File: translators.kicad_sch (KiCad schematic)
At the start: 53 parts, among them U10 SN74AXC8T245_UQFN, U2 SN74AXC8T245_UQFN, U3 SN74AXC8T245_UQFN, U4 SN74AXC8T245_UQFN, U5 SN74AXC8T245_UQFN, U6 SN74AXC8T245_UQFN

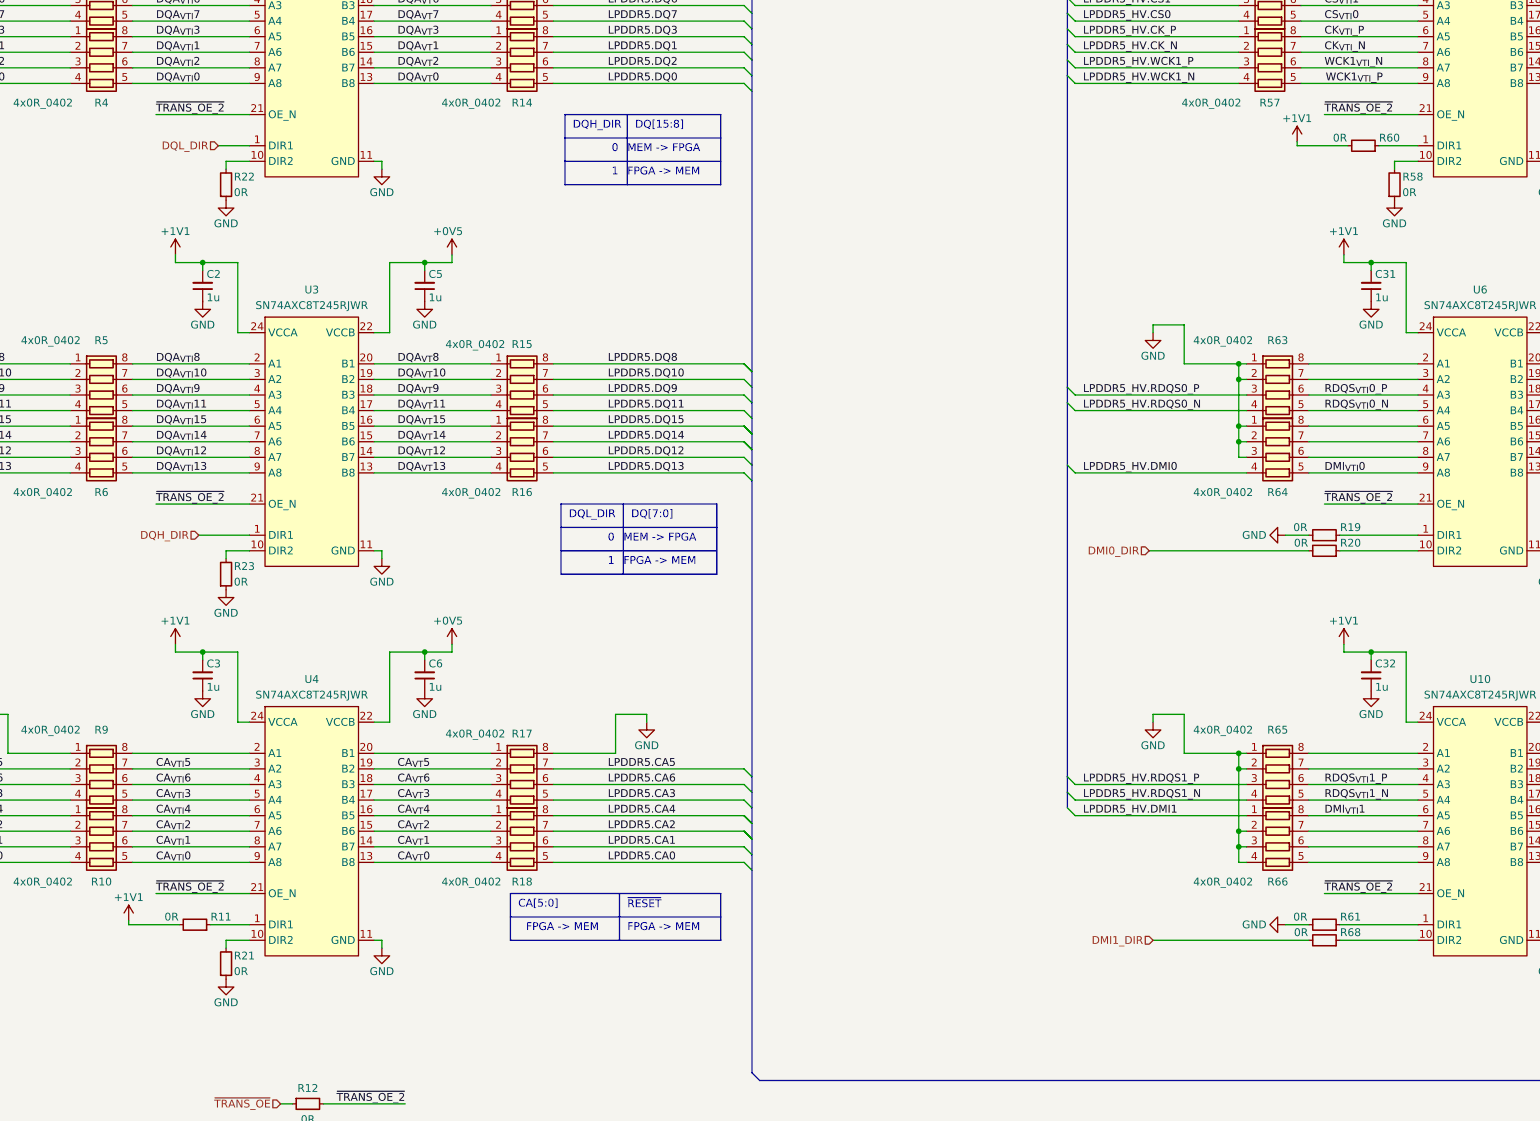
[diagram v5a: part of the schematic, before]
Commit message: [#52835] schematics: remove some 0R to simplify translator layout
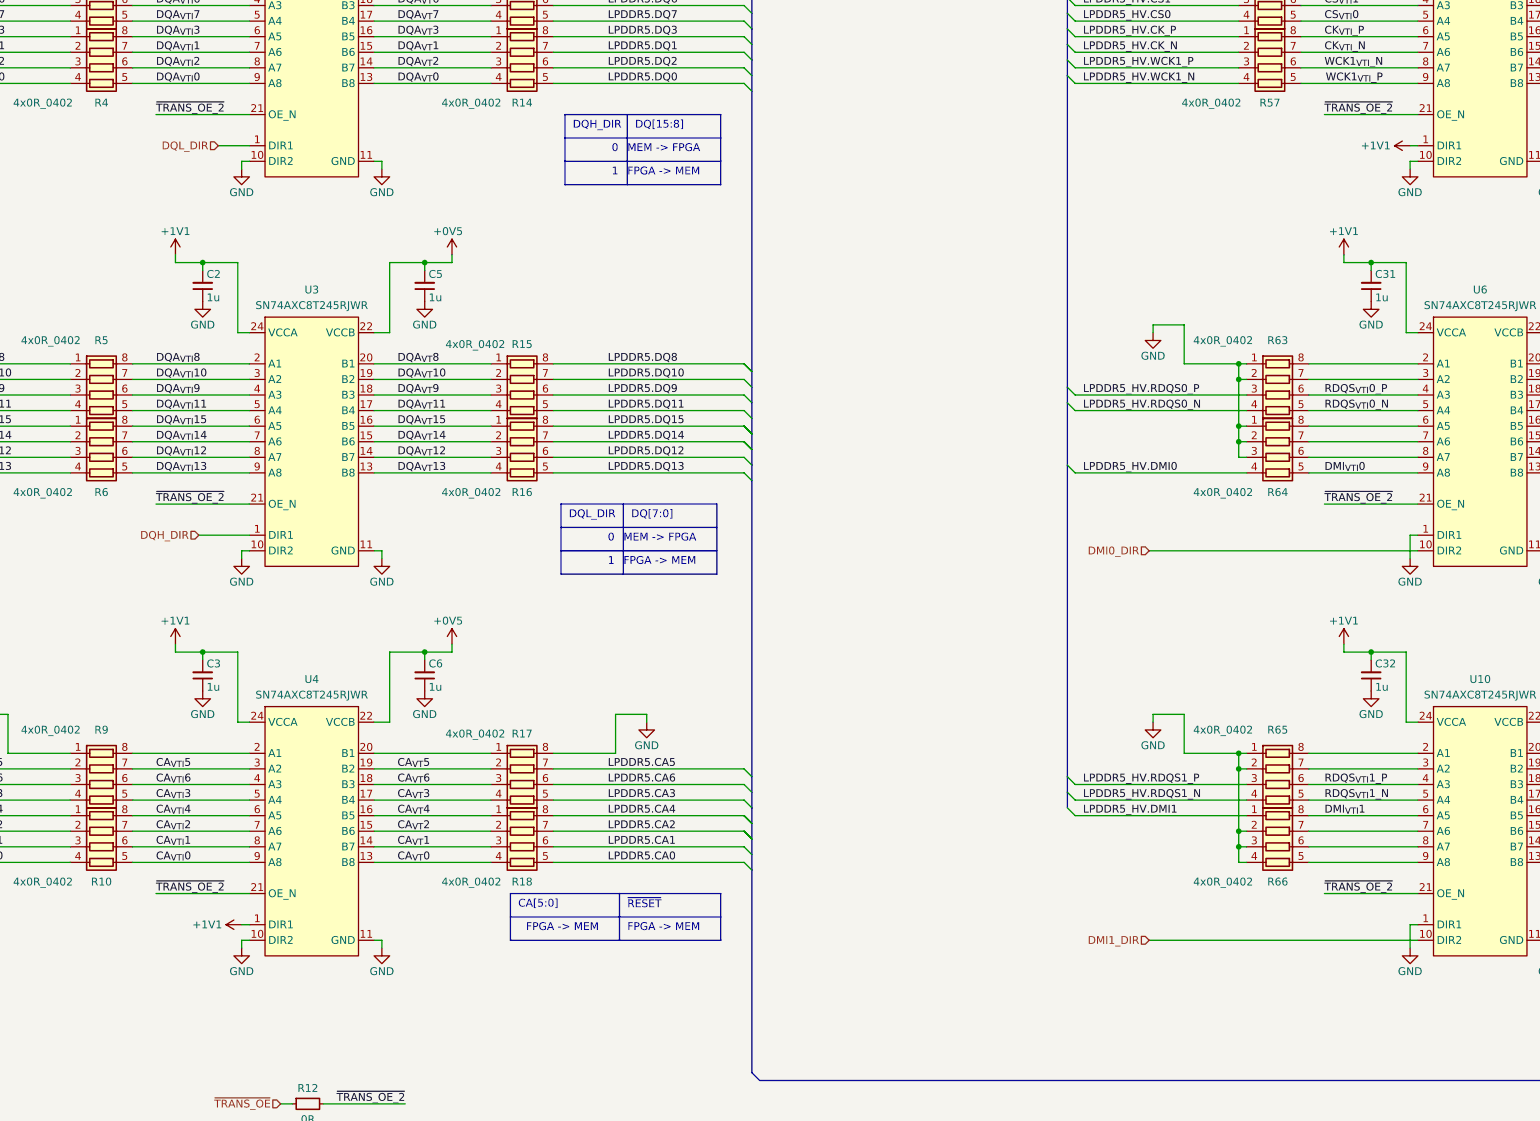
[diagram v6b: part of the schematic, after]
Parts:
- removed R11, R19, R20, R21, R22, R23, R58, R60, R61, R68: R_0R_0402, antmicro-footprints:R_0402_1005Metric, symbol antmicroResistors0402:R_0R_0402
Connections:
- net +1V1: now also U4.1 (DIR1), U5.1 (DIR1)
- net DMI0_DIR: now also U6.10 (DIR2)
- net DMI1_DIR: now also U10.10 (DIR2)
- net GND: now also U10.1 (DIR1), U2.10 (DIR2), U3.10 (DIR2), U4.10 (DIR2), U5.10 (DIR2), U6.1 (DIR1)

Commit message: [#52536] 52835: use resistors dividers instead of translators
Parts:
- removed C1, C2, C26, C3, C30, C31, C32, C33, C34, C4, C5, C6: C_1u_0402, antmicro-footprints:C_0402_1005Metric, symbol antmicroCapacitors0402:C_1u_0402
- removed R10, R13, R14, R15, R16, R17, R18, R24, R25, R3, R4, R48, R49, R5, R56, R57, R6, R63, R64, R65, R66, R7, R8, R9: 4x0R_0402_array, antmicro-footprints:4x0R_0402_array_EXB28V, symbol antmicroResistorNetworksArrays:4x0R_0402_array
- removed R12: R_0R_0402, antmicro-footprints:R_0402_1005Metric, symbol antmicroResistors0402:R_0R_0402
- removed U10, U2, U3, U4, U5, U6: SN74AXC8T245_UQFN, antmicro-footprints:UQFN-24_2x4mm_P0.4mm_Texas_RJW0024A, symbol antmicroLogicTranslatorsLevelShifters:SN74AXC8T245_UQFN
- added R15, R16, R17, R18, R19, R20, R21, R22, R23, R25, R3, R4, R49, R5, R54, R6, R64, R65, R66, R67, R7, R8: 4x100R_0201_array, antmicro-footprints:R_Array_4x0201_Panasonic_EXB18V, symbol antmicroResistorNetworksArrays:4x100R_0201_array
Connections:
- net GND: now also R18.5 (R4.2), R18.6 (R3.2), R18.7 (R2.2), R18.8 (R1.2), R25.1 (R1.1), R25.2 (R2.1), R25.3 (R3.1), R25.4 (R4.1), R3.5 (R4.2), R3.6 (R3.2), R3.7 (R2.2), R3.8 (R1.2), R4.1 (R1.1), R4.2 (R2.1), R4.3 (R3.1), R4.4 (R4.1), R49.1 (R1.1), R49.2 (R2.1), R49.3 (R3.1), R49.4 (R4.1), R5.1 (R1.1), R5.2 (R2.1), R5.3 (R3.1), R5.4 (R4.1), R6.1 (R1.1), R6.2 (R2.1), R6.3 (R3.1), R6.4 (R4.1), R66.1 (R1.1), R66.2 (R2.1), R66.3 (R3.1), R66.4 (R4.1), R67.1 (R1.1), R67.2 (R2.1), R67.3 (R3.1), R67.4 (R4.1), R7.1 (R1.1), R7.2 (R2.1), R7.3 (R3.1), R7.4 (R4.1), R8.1 (R1.1), R8.2 (R2.1), R8.3 (R3.1), R8.4 (R4.1)
- new net LPDDR5_DIE.CA0: R21.3 (R3.1), R5.6 (R3.2)
- new net LPDDR5_DIE.CA1: R21.4 (R4.1), R5.5 (R4.2)
- new net LPDDR5_DIE.CA2: R22.1 (R1.1), R6.8 (R1.2)
- new net LPDDR5_DIE.CA3: R22.2 (R2.1), R6.7 (R2.2)
- new net LPDDR5_DIE.CA4: R22.3 (R3.1), R6.6 (R3.2)
- new net LPDDR5_DIE.CA5: R22.4 (R4.1), R6.5 (R4.2)
- new net LPDDR5_DIE.CA6: R16.6 (R3.2), R3.3 (R3.1)
- new net LPDDR5_DIE.CK_N: R65.2 (R2.1), R67.7 (R2.2)
- new net LPDDR5_DIE.CK_P: R65.3 (R3.1), R67.6 (R3.2)
- new net LPDDR5_DIE.CS0: R20.4 (R4.1), R49.5 (R4.2)
- new net LPDDR5_DIE.CS1: R16.8 (R1.2), R3.1 (R1.1)
- new net LPDDR5_DIE.DMI0: R15.6 (R3.2), R18.3 (R3.1)
- new net LPDDR5_DIE.DMI1: R16.7 (R2.2), R3.2 (R2.1)
- new net LPDDR5_DIE.DQ0: R15.8 (R1.2), R18.1 (R1.1)
- new net LPDDR5_DIE.DQ1: R19.1 (R1.1), R25.8 (R1.2)
- new net LPDDR5_DIE.DQ10: R17.7 (R2.2), R4.7 (R2.2)
- new net LPDDR5_DIE.DQ11: R17.5 (R4.2), R4.5 (R4.2)
- new net LPDDR5_DIE.DQ12: R23.6 (R3.2), R7.6 (R3.2)
- new net LPDDR5_DIE.DQ13: R23.5 (R4.2), R7.5 (R4.2)
- new net LPDDR5_DIE.DQ14: R23.7 (R2.2), R7.7 (R2.2)
- new net LPDDR5_DIE.DQ15: R23.8 (R1.2), R7.8 (R1.2)
- new net LPDDR5_DIE.DQ2: R15.7 (R2.2), R18.2 (R2.1)
- new net LPDDR5_DIE.DQ3: R19.2 (R2.1), R25.7 (R2.2)
- new net LPDDR5_DIE.DQ4: R15.5 (R4.2), R18.4 (R4.1)
- new net LPDDR5_DIE.DQ5: R20.1 (R1.1), R49.8 (R1.2)
- new net LPDDR5_DIE.DQ6: R20.2 (R2.1), R49.7 (R2.2)
- new net LPDDR5_DIE.DQ7: R20.3 (R3.1), R49.6 (R3.2)
- new net LPDDR5_DIE.DQ8: R17.8 (R1.2), R4.8 (R1.2)
- new net LPDDR5_DIE.DQ9: R17.6 (R3.2), R4.6 (R3.2)
- new net LPDDR5_DIE.WCK0_N: R54.2 (R2.1), R8.7 (R2.2)
- new net LPDDR5_DIE.WCK0_P: R54.3 (R3.1), R8.6 (R3.2)
- new net LPDDR5_DIE.WCK1_N: R64.2 (R2.1), R66.7 (R2.2)
- new net LPDDR5_DIE.WCK1_P: R64.3 (R3.1), R66.6 (R3.2)
- new net LPDDR5_IN.CA0: R21.6 (R3.2)
- new net LPDDR5_IN.CA1: R21.5 (R4.2)
- new net LPDDR5_IN.CA2: R22.8 (R1.2)
- new net LPDDR5_IN.CA3: R22.7 (R2.2)
- new net LPDDR5_IN.CA4: R22.6 (R3.2)
- new net LPDDR5_IN.CA5: R22.5 (R4.2)
- new net LPDDR5_IN.CA6: R16.3 (R3.1)
- new net LPDDR5_IN.CK_N: R65.7 (R2.2)
- new net LPDDR5_IN.CK_P: R65.6 (R3.2)
- new net LPDDR5_IN.CS0: R20.5 (R4.2)
- new net LPDDR5_IN.CS1: R16.1 (R1.1)
- new net LPDDR5_IN.DMI0: R15.3 (R3.1)
- new net LPDDR5_IN.DMI1: R16.2 (R2.1)
- new net LPDDR5_IN.DQ0: R15.1 (R1.1)
- new net LPDDR5_IN.DQ1: R19.8 (R1.2)
- new net LPDDR5_IN.DQ10: R17.2 (R2.1)
- new net LPDDR5_IN.DQ11: R17.4 (R4.1)
- new net LPDDR5_IN.DQ12: R23.3 (R3.1)
- new net LPDDR5_IN.DQ13: R23.4 (R4.1)
- new net LPDDR5_IN.DQ14: R23.2 (R2.1)
- new net LPDDR5_IN.DQ15: R23.1 (R1.1)
- new net LPDDR5_IN.DQ2: R15.2 (R2.1)
- new net LPDDR5_IN.DQ3: R19.7 (R2.2)
- new net LPDDR5_IN.DQ4: R15.4 (R4.1)
- new net LPDDR5_IN.DQ5: R20.8 (R1.2)
- new net LPDDR5_IN.DQ6: R20.7 (R2.2)
- new net LPDDR5_IN.DQ7: R20.6 (R3.2)
- new net LPDDR5_IN.DQ8: R17.1 (R1.1)
- new net LPDDR5_IN.DQ9: R17.3 (R3.1)
- new net LPDDR5_IN.WCK0_N: R54.7 (R2.2)
- new net LPDDR5_IN.WCK0_P: R54.6 (R3.2)
- new net LPDDR5_IN.WCK1_N: R64.7 (R2.2)
- new net LPDDR5_IN.WCK1_P: R64.6 (R3.2)
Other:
- note removed: "0"
- note removed: "1"
- note removed: "CA[5:0]"
- note removed: "DMI0"
- note removed: "DMI0_DIR"
- note removed: "DMI1"
- note removed: "DQH_DIR"
- note removed: "DQL_DIR"
- note removed: "DQ[15:8]"
- note removed: "DQ[7:0]"
- note removed: "FPGA -> MEM"
- note removed: "MEM -> FPGA"
- note removed: "RDQS_0"
- note removed: "RDQS_1"
- note removed: "WCK, CS, CK, WCK"
- note removed: "~{RESET}"
